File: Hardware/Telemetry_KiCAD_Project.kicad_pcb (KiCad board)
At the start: 4 copper layers, 80 x 87.3 mm, 68 parts, among them J1 TX SPI Debug, J2 RX SPI Debug, J3 50Ω SMA Connector, J4 10118192-0001LF, J5 DB37_Male_MountingHoles, U1 STM32L562VET, U2 Si4463, U3 Si4463, U4 ADL5521, U5 RSD-897.500-942.500-1612-TR, U6 LM317T, U7 USBLC6-2SC6, Y1 32MHz, Y2 32MHz, Y3 32MHz

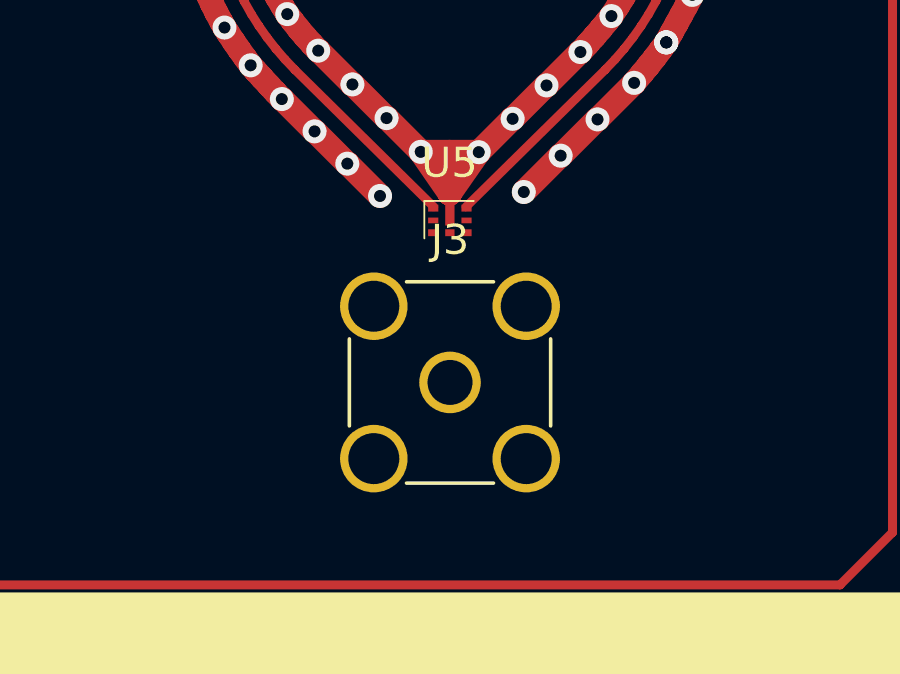
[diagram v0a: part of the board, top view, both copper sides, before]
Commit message: Improved via fence around sma connector
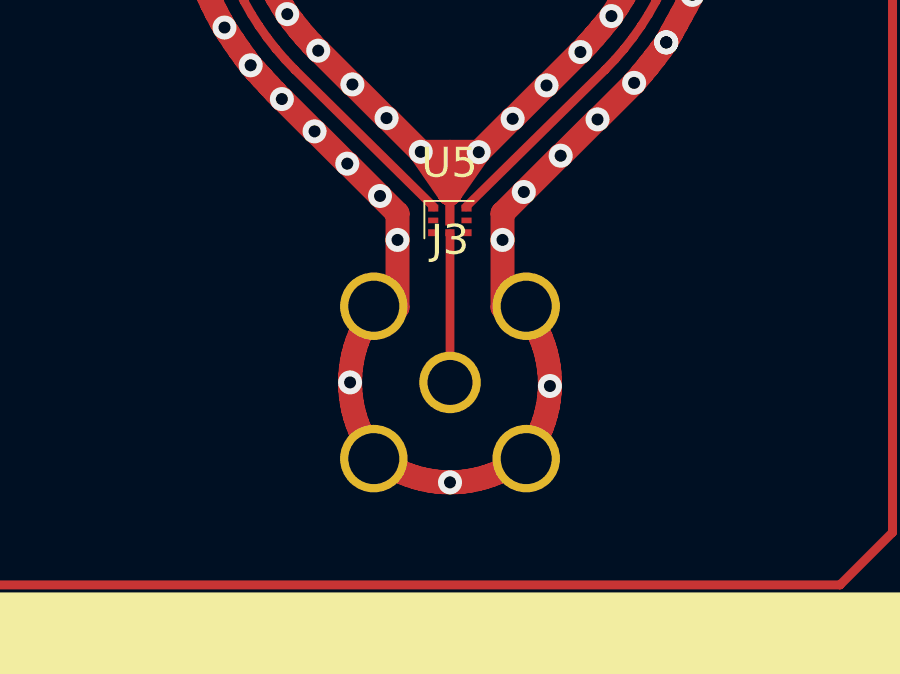
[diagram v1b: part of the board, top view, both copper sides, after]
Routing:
- net GND: track 113.1 -> 139.0 mm, vias 74 -> 79
- net /RSD_Duplexer/Antenna: track 0.00 -> 4.96 mm

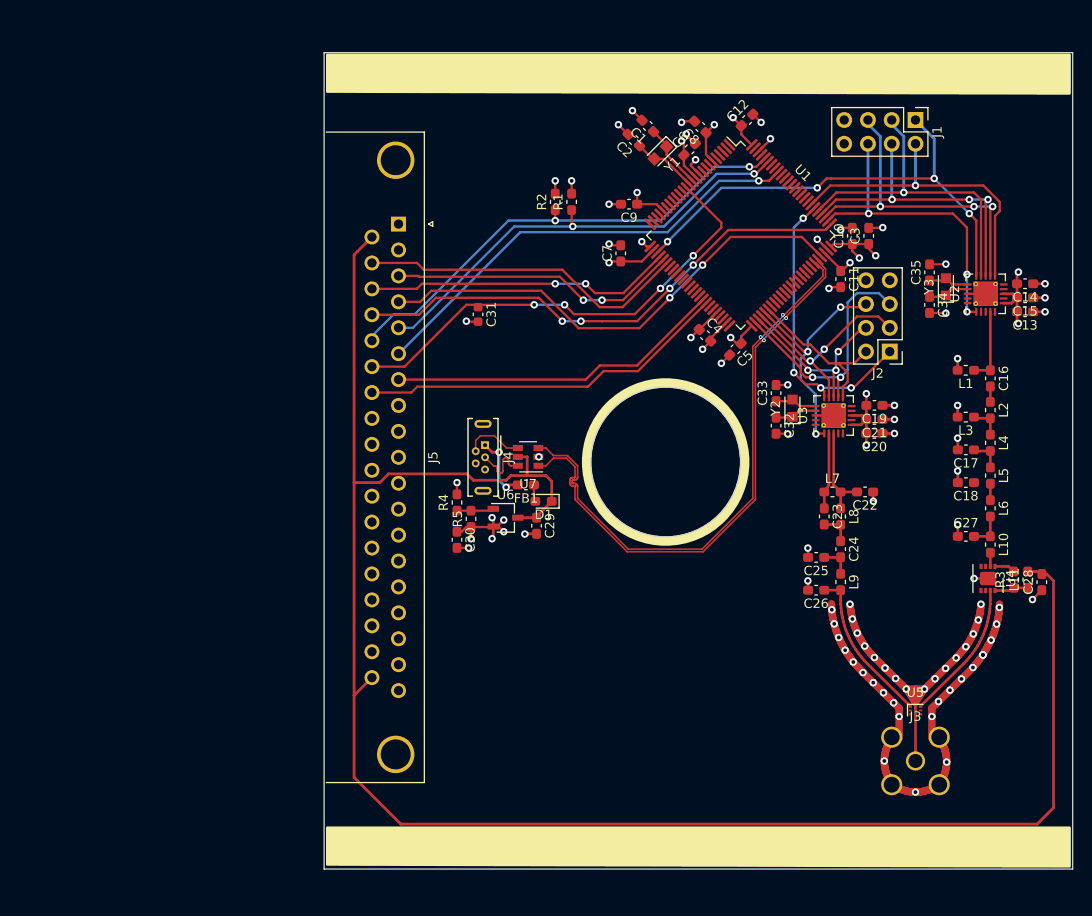
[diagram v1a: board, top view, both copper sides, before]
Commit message: Tidied up remaining ratsnest lines
Version 2 complete
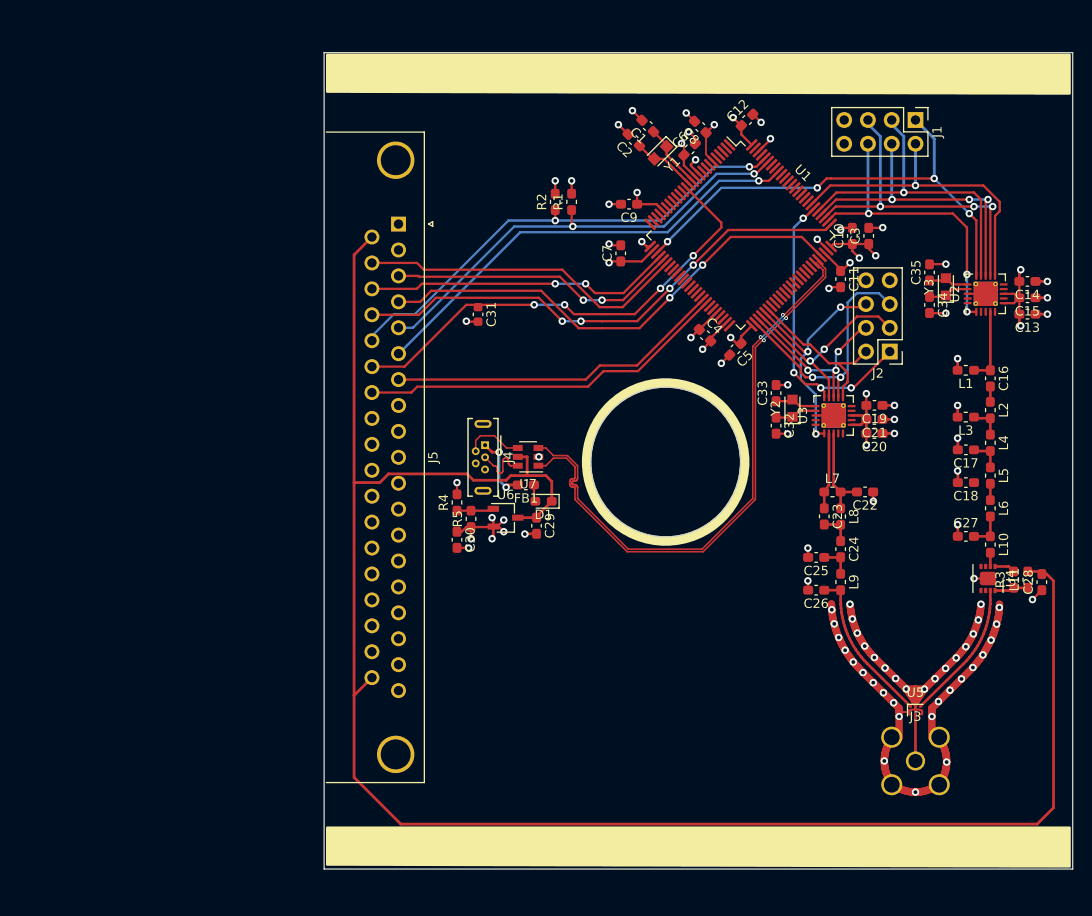
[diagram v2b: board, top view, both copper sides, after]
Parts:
- moved C13 0.35 mm to (182.0, 83.2)
- moved C14 0.35 mm to (182.0, 79.8)
- moved C15 0.25 mm to (182.0, 81.5)
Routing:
- net GND: track 139.0 -> 143.3 mm, vias 79 -> 78
- net Net-(R4-Pad1): track 3.46 -> 4.25 mm
- net +3V3: track 74.0 -> 74.7 mm

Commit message: Adjusted component silk screen, added pcb extensions
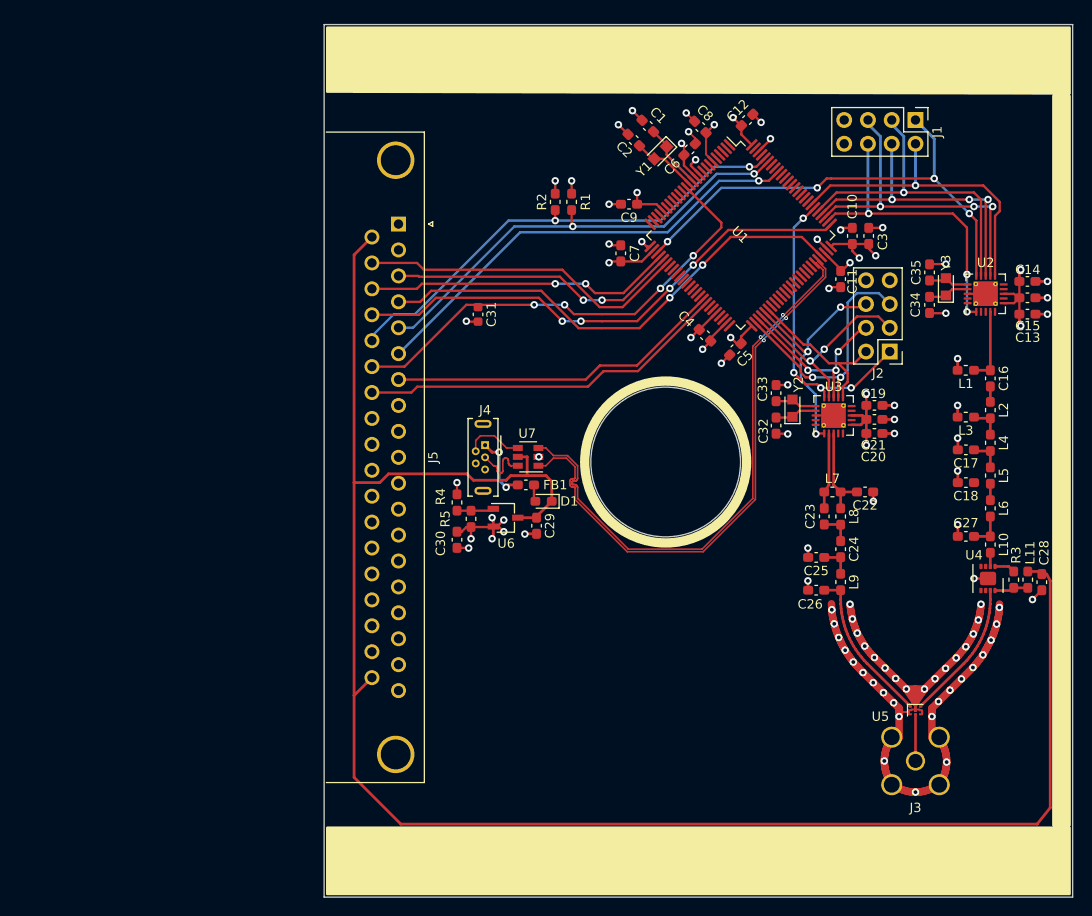
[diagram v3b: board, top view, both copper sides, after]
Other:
- board size 80 x 87.3 mm -> 80 x 93.3 mm

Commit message: Tweaked via fence connection to duplexer
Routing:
- net GND: track 143.3 -> 147.4 mm, vias 78 -> 79
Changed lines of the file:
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@@
     (thickness 1.6)
     (drawings 241)
-    (tracks 1040)
+    (tracks 1049)
     (zones 0)
     (modules 68)
@@
   )
   (setup
-    (last_trace_width 0.25)
+    (last_trace_width 0.8)
     (user_trace_width 0.1)
     (user_trace_width 0.2)
@@
   (via (at 173.216722 121.100205) (size 0.8) (drill 0.4) (layers F.Cu B.Cu) (net 2))
   (via (at 172.087243 122.21265) (size 0.8) (drill 0.4) (layers F.Cu B.Cu) (net 2))
-  (via (at 170.957764 123.325096) (size 0.8) (drill 0.4) (layers F.Cu B.Cu) (net 2) (status 1000000))
+  (via (at 170.957764 123.325096) (size 0.8) (drill 0.4) (layers F.Cu B.Cu) (net 2))
   (via (at 169.023665 123.314234) (size 0.8) (drill 0.4) (layers F.Cu B.Cu) (net 2))
   (via (at 167.884849 122.190171) (size 0.8) (drill 0.4) (layers F.Cu B.Cu) (net 2))
@@
   (segment (start 161.05619 114.836542) (end 161.02 114.2) (width 0.8) (layer F.Cu) (net 2))
   (segment (start 170.946902 123.314234) (end 170.957764 123.325096) (width 0.8) (layer F.Cu) (net 2))
-  (segment (start 169.99 124.71) (end 170.957764 123.325096) (width 0.8) (layer F.Cu) (net 2))
-  (segment (start 169.023665 123.314234) (end 169.99 124.71) (width 0.8) (layer F.Cu) (net 2))
-  (segment (start 169.994234 124.705766) (end 169.99 124.71) (width 0.8) (layer F.Cu) (net 2))
   (segment (start 169.023665 123.314234) (end 169.994234 123.314234) (width 0.8) (layer F.Cu) (net 2))
-  (segment (start 169.994234 123.314234) (end 169.994234 124.705766) (width 0.8) (layer F.Cu) (net 2))
   (segment (start 169.994234 123.314234) (end 170.946902 123.314234) (width 0.8) (layer F.Cu) (net 2))
   (via (at 122 84) (size 0.8) (drill 0.4) (layers F.Cu B.Cu) (net 2))
@@
   (via (at 145.75 63.75) (size 0.8) (drill 0.4) (layers F.Cu B.Cu) (net 2))
   (segment (start 146.46976 65.03024) (end 146.46976 64.46976) (width 0.2) (layer F.Cu) (net 2))
+  (segment (start 169.94 124.59) (end 169.94 125.1) (width 0.2) (layer F.Cu) (net 2))
+  (segment (start 170.05 124.57) (end 170.05 125.1) (width 0.2) (layer F.Cu) (net 2))
+  (segment (start 168.85 123.5) (end 169.94 124.59) (width 0.3) (layer F.Cu) (net 2))
+  (segment (start 171.12 123.52) (end 170.05 124.57) (width 0.3) (layer F.Cu) (net 2))
+  (segment (start 169.234234 123.314234) (end 169.94 124.02) (width 0.8) (layer F.Cu) (net 2))
+  (segment (start 169.023665 123.314234) (end 169.234234 123.314234) (width 0.8) (layer F.Cu) (net 2))
+  (segment (start 169.94 124.02) (end 169.94 124.59) (width 0.2) (layer F.Cu) (net 2))
+  (segment (start 169.94 123.39) (end 169.94 124.02) (width 0.2) (layer F.Cu) (net 2))
+  (segment (start 170.634904 123.325096) (end 169.94 124.02) (width 0.8) (layer F.Cu) (net 2))
+  (segment (start 170.957764 123.325096) (end 170.634904 123.325096) (width 0.8) (layer F.Cu) (net 2))
+  (segment (start 169.99 124.28) (end 170.05 124.57) (width 0.2) (layer F.Cu) (net 2))
+  (segment (start 170.05 123.51) (end 169.99 124.28) (width 0.2) (layer F.Cu) (net 2))
+  (via (at 169.99 124.28) (size 0.8) (drill 0.4) (layers F.Cu B.Cu) (net 2))
   (segment (start 178 106.999999) (end 178 104.874999) (width 0.29337) (layer F.Cu) (net 3))
   (segment (start 178 106.999999) (end 176.25 106.999999) (width 0.29337) (layer F.Cu) (net 3))

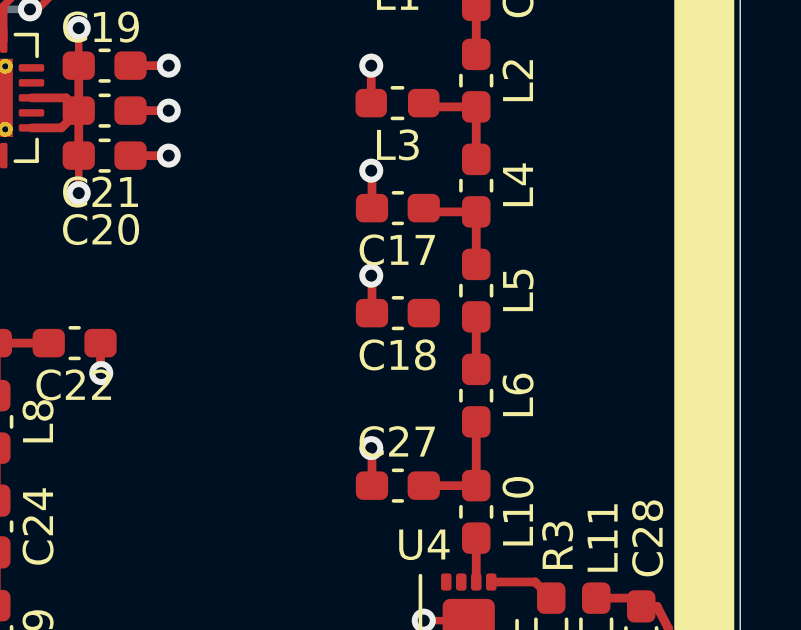
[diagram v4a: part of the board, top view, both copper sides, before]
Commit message: Connected C18 to L5
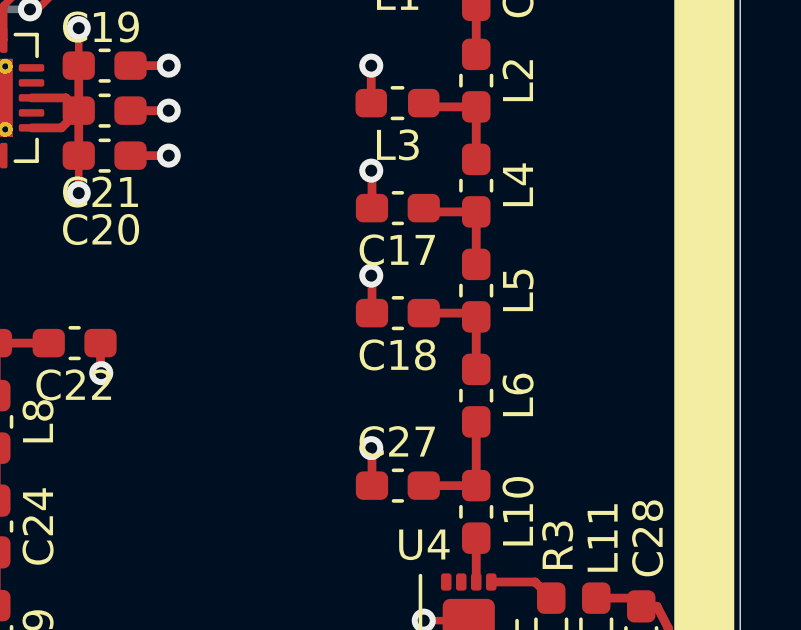
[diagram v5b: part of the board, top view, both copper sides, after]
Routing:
- net Net-(C18-Pad1): track 1.75 -> 3.55 mm
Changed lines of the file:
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@@
     (thickness 1.6)
     (drawings 241)
-    (tracks 1049)
+    (tracks 1051)
     (zones 0)
     (modules 68)
@@
   )
   (setup
-    (last_trace_width 0.8)
+    (last_trace_width 0.29337)
     (user_trace_width 0.1)
     (user_trace_width 0.2)
@@
   (segment (start 178 97.875) (end 176.4875 97.875) (width 0.29337) (layer F.Cu) (net 98))
   (segment (start 178 103.125001) (end 178 101.375) (width 0.29337) (layer F.Cu) (net 99))
+  (segment (start 177.875 101.25) (end 178 101.375) (width 0.29337) (layer F.Cu) (net 99))
+  (segment (start 176.25 101.25) (end 177.875 101.25) (width 0.29337) (layer F.Cu) (net 99))
   (segment (start 162 102.25) (end 162 104) (width 0.29337) (layer F.Cu) (net 100))
   (segment (start 162 102.25) (end 163.750001 102.249999) (width 0.29337) (layer F.Cu) (net 100))
